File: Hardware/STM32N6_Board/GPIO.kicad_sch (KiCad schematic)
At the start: 1 part

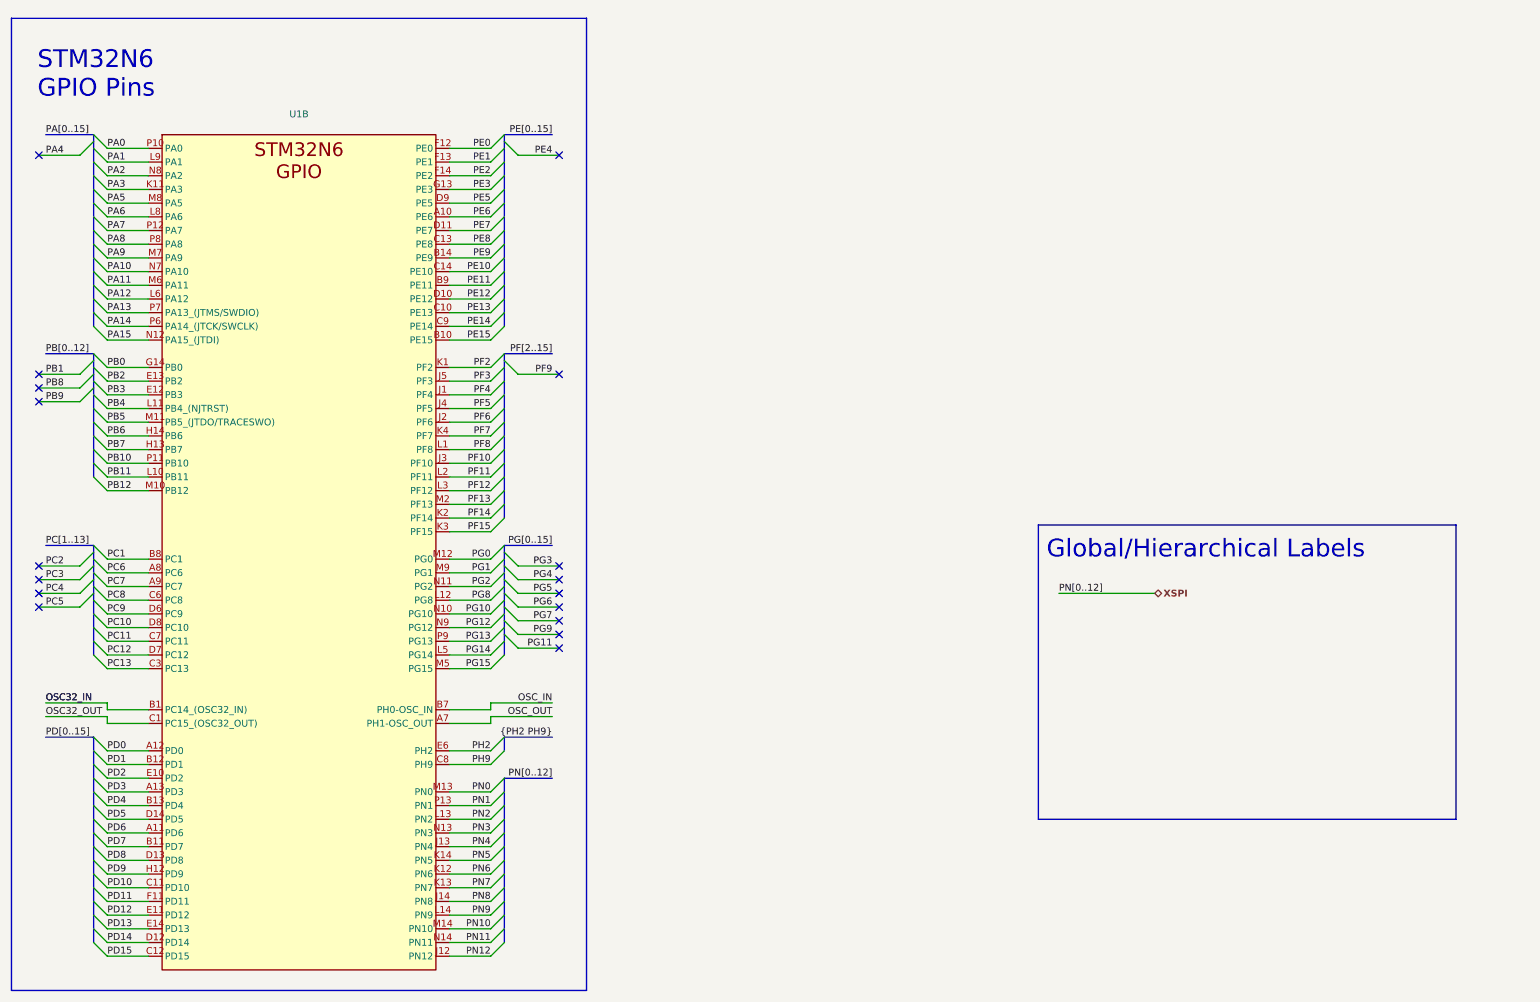
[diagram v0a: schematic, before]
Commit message: Completed wiring of the Analog unit.
- CSI and USB buses are created, yet to be connected with connectors
- Next will be pin selection, and drawing in FMC SDRAM
- Then will be routing GPIOs as buses, and connecting with connectors
- Finally, board layout.
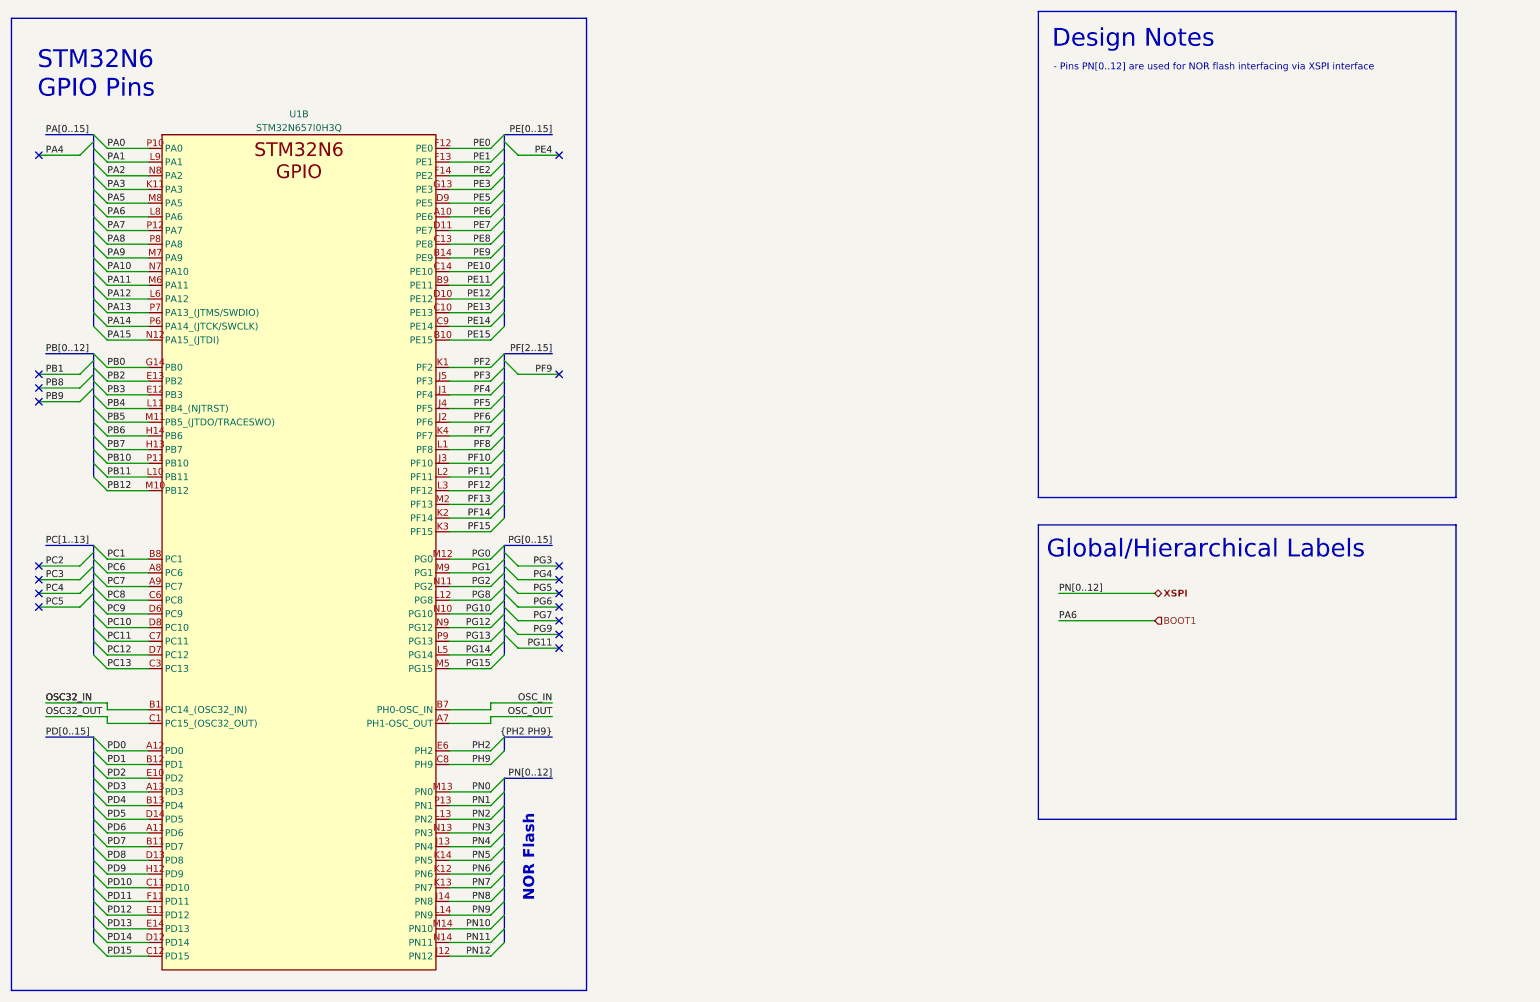
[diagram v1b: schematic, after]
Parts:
- U1: value ~ -> STM32N657I0H3Q
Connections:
- net PA6 renamed BOOT1
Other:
- note added: "- Pins PN[0..12] are used for NOR flash interfacing via XSPI interface"
- note added: "Design Notes"
- note added: "NOR Flash"
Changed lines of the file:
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@@
 	)
 	(rectangle
+		(start 205.74 13.97)
+		(end 283.21 104.14)
+		(stroke
+			(width 0.254)
+			(type solid)
+		)
+		(fill
+			(type none)
+		)
+	)
+	(rectangle
 		(start 15.24 15.24)
 		(end 121.92 195.58)
@@
 		)
 	)
+	(text "- Pins PN[0..12] are used for NOR flash interfacing via XSPI interface"
+		(exclude_from_sim no)
+		(at 208.534 23.622 0)
+		(effects
+			(font
+				(size 1.27 1.27)
+				(thickness 0.1588)
+			)
+			(justify left top)
+		)
+	)
 	(text "STM32N6\nGPIO Pins"
 		(exclude_from_sim no)
@@
 		)
 	)
+	(text "NOR Flash"
+		(exclude_from_sim no)
+		(at 111.252 179.07 90)
+		(effects
+			(font
+				(size 2.032 2.032)
+				(thickness 0.254)
+				(bold yes)
+			)
+			(justify left)
+		)
+	)
+	(text "Design Notes"
+		(exclude_from_sim no)
+		(at 208.28 19.05 0)
+		(effects
+			(font
+				(size 3.302 3.302)
+				(thickness 0.4128)
+			)
+			(justify left)
+		)
+	)
 	(no_connect
 		(at 116.84 132.08)
@@
 		)
 	)
+	(wire
+		(pts
+			(xy 209.55 127) (xy 227.33 127)
+		)
+		(stroke
+			(width 0)
+			(type default)
+		)
+	)
 	(bus
 		(pts
@@
 		)
 	)
+	(label "PA6"
+		(at 209.55 127 0)
+		(effects
+			(font
+				(size 1.27 1.27)
+			)
+			(justify left bottom)
+		)
+	)
 	(label "PE8"
 		(at 104.14 57.15 180)
@@
 		)
 	)
+	(hierarchical_label "BOOT1"
+		(shape input)
+		(at 227.33 127 0)
+		(effects
+			(font
+				(size 1.27 1.27)
+			)
+			(justify left)
+		)
+	)
 	(symbol
 		(lib_id "STM32N6_Symbols:STM32N657I0H3Q")
@@
 			)
 		)
-		(property "Value" "~"
+		(property "Value" "STM32N657I0H3Q"
 			(at 68.58 35.56 0)
 			(effects

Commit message: Added pinout to GPIO
- Had to rearrange the pinout a little, due to SPI NSS issue
- New pinout updated in google spreadsheet and image in docs
- Added buses in GPIO sheet, as well as all necessary labels
- Next is wiring in FMC SDRAM, and connectors.
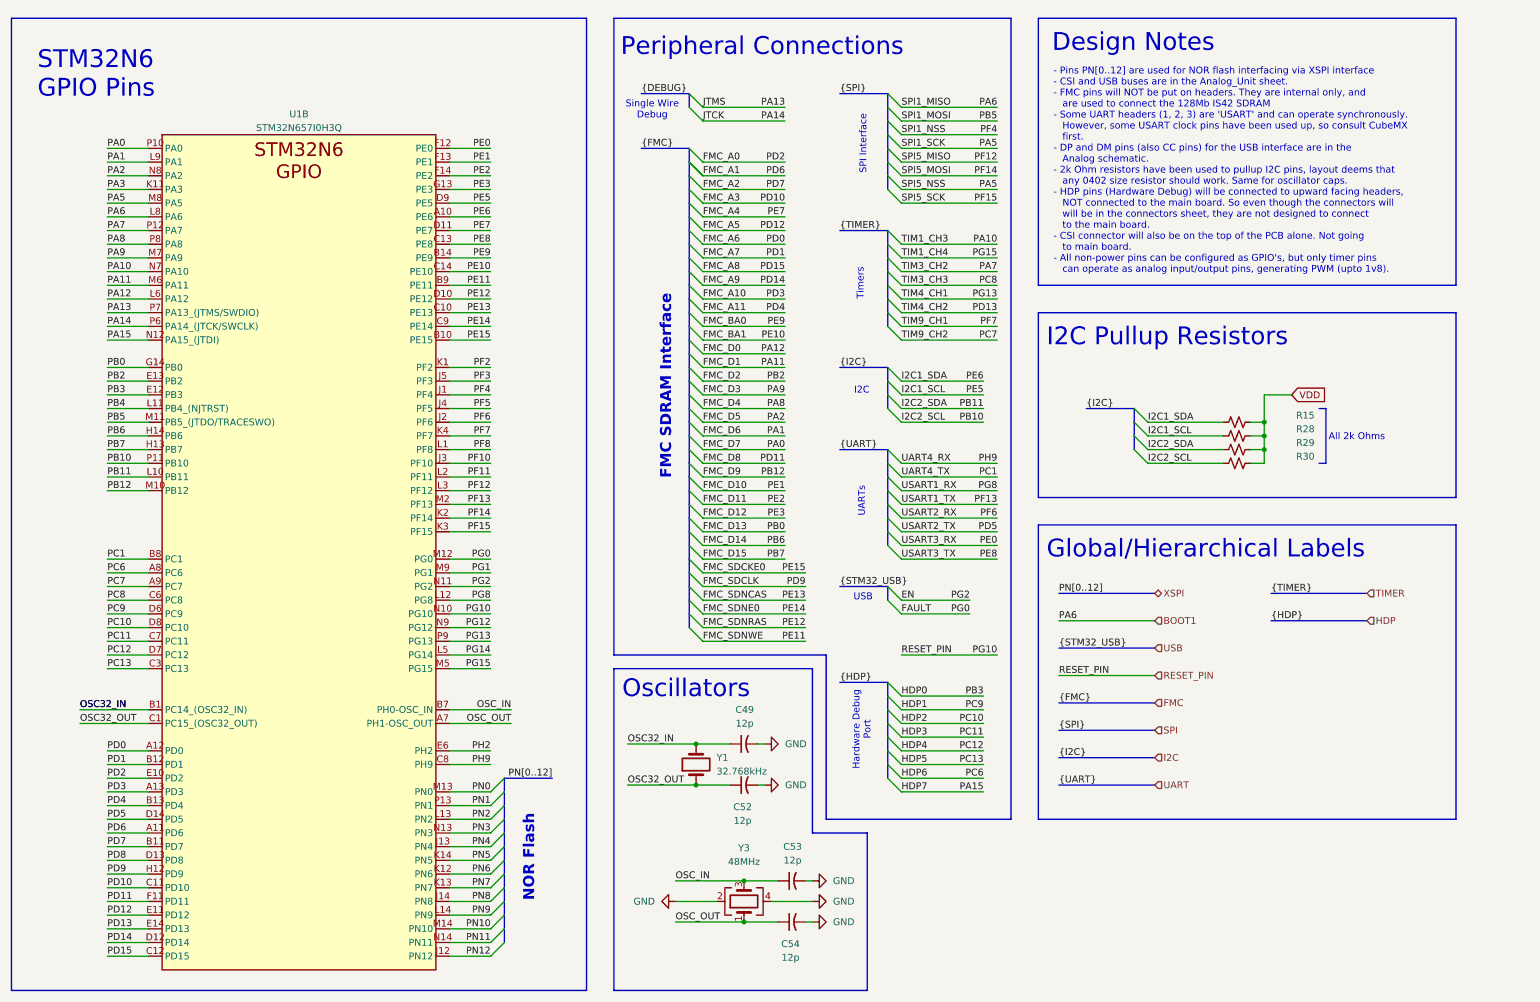
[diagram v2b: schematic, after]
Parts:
- added C49, C52, C53, C54: 12p, symbol Device:C_Small_US
- added R15, R28, R29, R30: 2k, symbol Device:R_Small_US
- added Y1: 32.768kHz, symbol Device:Crystal
- added Y3: 48MHz, symbol Device:Crystal_GND24
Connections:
- net OSC32_IN: now also C49.1, Y1.2
- net OSC32_OUT: now also C52.1, Y1.1
- net OSC_IN: now also C53.1, Y3.3
- net OSC_OUT: now also C54.1, Y3.1
- net PA0 renamed FMC_D7
- net PA1 renamed FMC_D6
- net PA11 renamed FMC_D1
- net PA12 renamed FMC_D0
- net PA13 renamed JTMS
- net PA14 renamed JTCK
- net PA15 renamed HDP7
- net PA2 renamed FMC_D5
- net PA8 renamed FMC_D4
- net PA9 renamed FMC_D3
- net PB0 renamed FMC_D13
- net PB10 renamed I2C2_SCL
- net I2C2_SCL: now also R30.1
- net PB11 renamed I2C2_SDA
- net I2C2_SDA: now also R29.1
- net PB12 renamed FMC_D9
- net PB2 renamed FMC_D2
- net PB3 renamed HDP0
- net PB6 renamed FMC_D14
- net PB7 renamed FMC_D15
- net PC10 renamed HDP2
- net PC11 renamed HDP3
- net PC12 renamed HDP4
- net PC13 renamed HDP5
- net PC6 renamed HDP6
- net PC9 renamed HDP1
- net PD0 renamed FMC_A6
- net PD1 renamed FMC_A7
- net PD10 renamed FMC_A3
- net PD11 renamed FMC_D8
- net PD12 renamed FMC_A5
- net PD14 renamed FMC_A9
- net PD15 renamed FMC_A8
- net PD2 renamed FMC_A0
- net PD3 renamed FMC_A10
- net PD4 renamed FMC_A11
- net PD6 renamed FMC_A1
- net PD7 renamed FMC_A2
- net PD9 renamed FMC_SDCLK
- net PE1 renamed FMC_D10
- net PE10 renamed FMC_BA1
- net PE11 renamed FMC_SDNWE
- net PE12 renamed FMC_SDNRAS
- net PE13 renamed FMC_SDNCAS
- net PE14 renamed FMC_SDNE0
- net PE15 renamed FMC_SDCKE0
- net PE2 renamed FMC_D11
- net PE3 renamed FMC_D12
- net PE5 renamed I2C1_SCL
- net I2C1_SCL: now also R28.1
- net PE6 renamed I2C1_SDA
- net I2C1_SDA: now also R15.1
- net PE7 renamed FMC_A4
- net PE9 renamed FMC_BA0
- net PG0 renamed FAULT
- net PG10 renamed RESET_PIN
- net PG2 renamed EN
- new net GND: C49.2, C52.2, C53.2, C54.2, Y3.2, Y3.4
- new net VDD: R15.2, R28.2, R29.2, R30.2
- no-connect marks 17 -> 0
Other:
- note added: "- Pins PN[0..12] are used for NOR flash interfacing via XSPI interface - CSI and USB buses are in the Analog_Unit sheet. - FMC pins will NOT be put on headers. They are internal only, and are used to connect the 128Mb IS42 SDRAM - Some UART headers (1, 2, 3) are 'USART' and can operate synchronously. However, some USART clock pins have been used up, so consult CubeMX first. - DP and DM pins (also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"
- note added: "All 2k Ohms"
- note added: "FMC SDRAM Interface"
- note added: "Hardware Debug Port"
- note added: "I2C"
- note added: "I2C Pullup Resistors"
- note added: "Oscillators"
- note added: "Peripheral Connections"
- note added: "SPI Interface"
- note added: "Single Wire Debug"
- note added: "Timers"
- note added: "UARTs"
- note added: "USB"
- note removed: "- Pins PN[0..12] are used for NOR flash interfacing via XSPI interface"

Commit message: Completed the schematic.
- The schematic is complete.
- ERC checker, footprint assignment, and PCB board design left
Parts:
- added D6: LED_Small, symbol Device:LED_Small
- added R31: 200, symbol Device:R_Small_US
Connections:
- net PA7 is gone; now on net HDP7: U1.P12 (PA7)
- net PC8 is gone; now on net HDP0: U1.C6 (PC8)
- net RESET_PIN is gone; now on net EN: U1.N10 (PG10)
- net GND: now also R31.2
- net HDP0: no longer U1.E12 (PB3)
- net HDP7: no longer U1.N12 (PA15_(JTDI))
- net JTCK renamed PA14
- net JTMS renamed PA13
- net PB4 renamed LED_BUILTIN
- net LED_BUILTIN: now also D6.2 (A)
- net PD8 renamed FMC_NBL0
- new net: D6.1 (K), R31.1
- new net FMC_NBL1: U1.E12 (PB3)
- new net PA15: U1.N12 (PA15_(JTDI))
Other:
- moved on the sheet: C49, C52, C53, C54, Y1, Y3

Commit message: Made fixes to remove ERC errors
- 1 remaining error, but > 100 warnings D:
- The remaining error is a bug within KiCAD I believe
- Next is footprint assignment
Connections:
- net FMC_SDNCAS renamed FMC_SKNCAS
- no-connect marks 0 -> 11
